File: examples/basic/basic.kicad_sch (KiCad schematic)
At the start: 4 parts

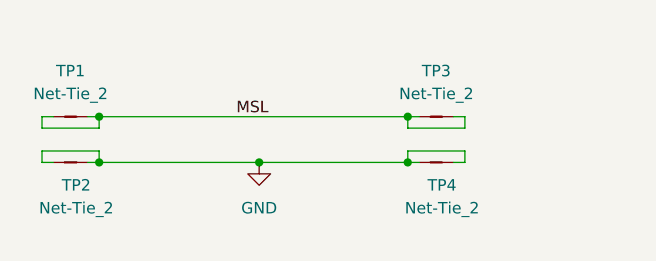
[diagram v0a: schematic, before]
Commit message: Update examples with corrected settings and keep track of exported gerbers
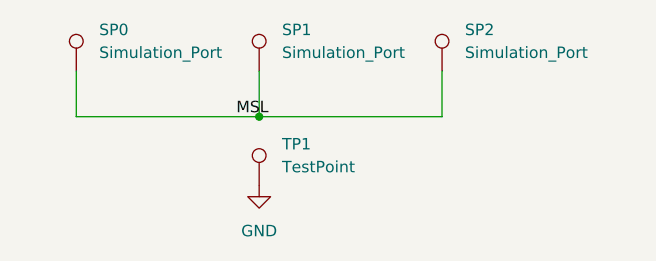
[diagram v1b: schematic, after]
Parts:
- removed TP1, TP2, TP3, TP4: Net-Tie_2, antmicro-footprints:NetTie-2_SMD_Pad0.127mm, symbol antmicroShuntsJumpers:Net-Tie_2
- added SP0, SP1, SP2: Simulation_Port, simulation_port:pad_0.4mm, symbol Connector:TestPoint
- added TP1: TestPoint, simulation_port:pad_0.1mm, symbol Connector:TestPoint
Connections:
- net GND: now also TP1.1
- net MSL: now also SP0.1, SP1.1, SP2.1
